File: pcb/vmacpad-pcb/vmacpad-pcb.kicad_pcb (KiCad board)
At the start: 2 copper layers, 134.7 x 126.1 mm, 79 parts, among them J1 TYPE-C-31-M12_13, J2 Conn_01x04_Pin, J3 Conn_01x04_Pin, K1 1u, K10 1u, K12 2.25u, K13 1u, K14 1u, K16 1u, K17 1u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

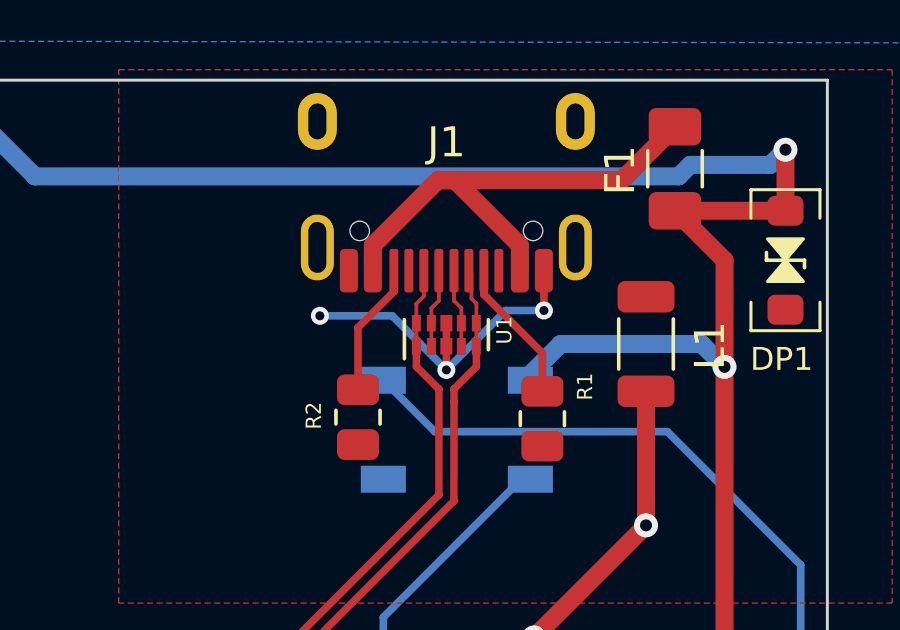
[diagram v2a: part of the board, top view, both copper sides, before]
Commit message: FIX USB connection
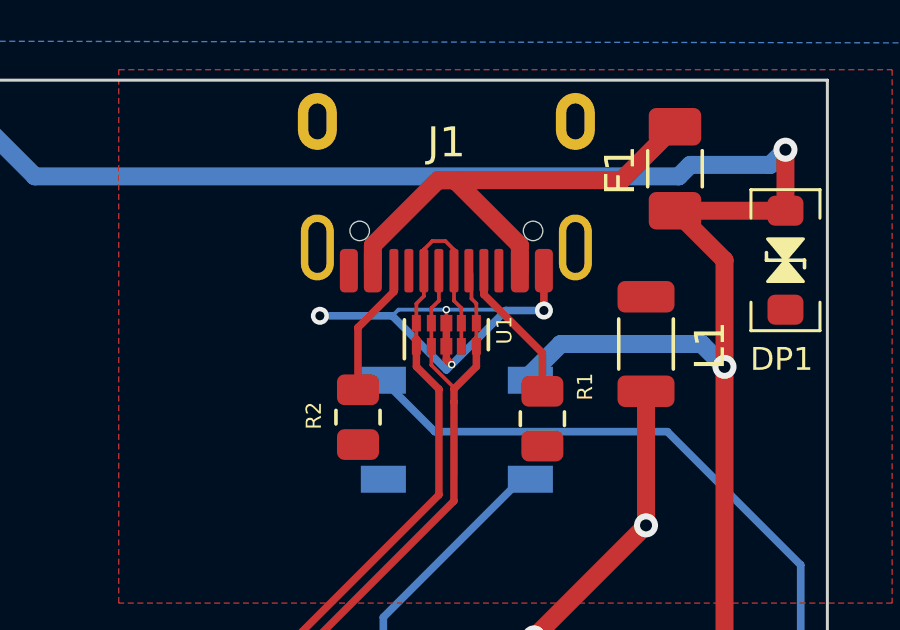
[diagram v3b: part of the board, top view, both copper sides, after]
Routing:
- net GNDPWR: track 11.9 -> 16.1 mm, vias 3 -> 4
- net USB+: track 158.8 -> 161.5 mm
- net USB-: track 159.5 -> 161.3 mm
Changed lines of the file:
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@@
   (via (at 130.7325 181.991) (size 0.6) (drill 0.3) (layers "F.Cu" "B.Cu") (net 3))
   (segment (start 114.3 196.342) (end 114.3 196.215) (width 0.254) (layer "B.Cu") (net 3))
+  (segment (start 211.582 106.7562) (end 211.582 107.188) (width 0.254) (layer "F.Cu") (net 4))
   (segment (start 214.8332 105.5624) (end 214.8332 104.2367) (width 0.254) (layer "F.Cu") (net 4))
   (segment (start 214.8332 104.2367) (end 214.832 104.2355) (width 0.254) (layer "F.Cu") (net 4))
+  (segment (start 211.582 105.536615) (end 211.58015 105.534765) (width 0.127) (layer "F.Cu") (net 4))
+  (segment (start 211.582 105.9862) (end 211.582 105.536615) (width 0.127) (layer "F.Cu") (net 4))
   (segment (start 211.582 106.7562) (end 211.582 105.9862) (width 0.254) (layer "F.Cu") (net 4))
-  (segment (start 211.582 106.7562) (end 211.582 107.5436) (width 0.254) (layer "F.Cu") (net 4))
+  (segment (start 211.582 107.188) (end 211.7598 107.3658) (width 0.254) (layer "F.Cu") (net 4))
   (via (at 214.8332 105.5624) (size 0.6) (drill 0.3) (layers "F.Cu" "B.Cu") (net 4))
   (via (at 207.3656 105.7402) (size 0.6) (drill 0.3) (layers "F.Cu" "B.Cu") (net 4))
-  (via (at 211.582 107.5436) (size 0.6) (drill 0.3) (layers "F.Cu" "B.Cu") (net 4))
+  (via (at 211.58015 105.534765) (size 0.25) (drill 0.15) (layers "F.Cu" "B.Cu") (net 4))
+  (via (at 211.7598 107.3658) (size 0.25) (drill 0.15) (layers "F.Cu" "B.Cu") (net 4))
   (segment (start 211.582 107.5436) (end 209.7786 105.7402) (width 0.254) (layer "B.Cu") (net 4))
-  (segment (start 211.582 107.5436) (end 213.5632 105.5624) (width 0.254) (layer "B.Cu") (net 4))
+  (segment (start 213.535565 105.534765) (end 213.5632 105.5624) (width 0.127) (layer "B.Cu") (net 4))
+  (segment (start 211.582 107.5436) (end 211.7598 107.3658) (width 0.254) (layer "B.Cu") (net 4))
   (segment (start 209.7786 105.7402) (end 207.3656 105.7402) (width 0.254) (layer "B.Cu") (net 4))
+  (segment (start 211.58015 105.534765) (end 209.984035 105.534765) (width 0.127) (layer "B.Cu") (net 4))
   (segment (start 213.5632 105.5624) (end 214.8332 105.5624) (width 0.254) (layer "B.Cu") (net 4))
+  (segment (start 211.7598 107.3658) (end 213.5632 105.5624) (width 0.254) (layer "B.Cu") (net 4))
+  (segment (start 211.58015 105.534765) (end 213.535565 105.534765) (width 0.127) (layer "B.Cu") (net 4))
+  (segment (start 209.984035 105.534765) (end 209.7786 105.7402) (width 0.127) (layer "B.Cu") (net 4))
   (segment (start 214.7824 108.2567) (end 214.7824 106.979414) (width 0.254) (layer "F.Cu") (net 5))
   (segment (start 212.832 105.029014) (end 212.832 104.2355) (width 0.254) (layer "F.Cu") (net 5))
@@
   (segment (start 210.582 105.3342) (end 210.582 105.7362) (width 0.127) (layer "F.Cu") (net 77))
   (segment (start 196.7016 126.337646) (end 211.333502 111.705744) (width 0.25) (layer "F.Cu") (net 77))
+  (segment (start 210.832 103.531789) (end 210.832 104.2355) (width 0.127) (layer "F.Cu") (net 77))
   (segment (start 120.2984 165.860046) (end 125.880446 160.278) (width 0.25) (layer "F.Cu") (net 77))
   (segment (start 196.7016 144.879646) (end 196.7016 126.337646) (width 0.25) (layer "F.Cu") (net 77))
+  (segment (start 211.116789 103.247) (end 210.832 103.531789) (width 0.127) (layer "F.Cu") (net 77))
   (segment (start 212.082 105.4842) (end 212.082 105.9862) (width 0.127) (layer "F.Cu") (net 77))
   (segment (start 181.303246 160.278) (end 196.7016 144.879646) (width 0.25) (layer "F.Cu") (net 77))
@@
   (segment (start 210.582 107.4326) (end 210.582 106.5062) (width 0.25) (layer "F.Cu") (net 77))
   (segment (start 210.582 105.7362) (end 210.582 106.5062) (width 0.127) (layer "F.Cu") (net 77))
+  (segment (start 211.836 104.2355) (end 211.836 103.535789) (width 0.127) (layer "F.Cu") (net 77))
   (segment (start 210.832 105.0842) (end 210.582 105.3342) (width 0.127) (layer "F.Cu") (net 77))
   (segment (start 115.2125 185.86875) (end 118.425296 185.86875) (width 0.25) (layer "F.Cu") (net 77))
+  (segment (start 211.547211 103.247) (end 211.116789 103.247) (width 0.127) (layer "F.Cu") (net 77))
   (segment (start 211.333502 108.184102) (end 210.582 107.4326) (width 0.25) (layer "F.Cu") (net 77))
   (segment (start 211.836 104.2355) (end 211.836 105.2382) (width 0.127) (layer "F.Cu") (net 77))
+  (segment (start 211.836 103.535789) (end 211.547211 103.247) (width 0.127) (layer "F.Cu") (net 77))
   (segment (start 211.836 105.2382) (end 212.082 105.4842) (width 0.127) (layer "F.Cu") (net 77))
   (segment (start 212.082 105.9862) (end 212.082 106.7562) (width 0.127) (layer "F.Cu") (net 77))
@@
   (segment (start 210.832 104.2355) (end 210.832 105.0842) (width 0.127) (layer "F.Cu") (net 77))
   (segment (start 212.4185 105.167764) (end 212.4185 104.322) (width 0.127) (layer "F.Cu") (net 78))
+  (segment (start 211.082 107.383178) (end 211.836 108.137178) (width 0.127) (layer "F.Cu") (net 78))
   (segment (start 118.632404 186.36875) (end 120.7984 184.202754) (width 0.25) (layer "F.Cu") (net 78))
   (segment (start 211.332 105.2342) (end 211.082 105.4842) (width 0.127) (layer "F.Cu") (net 78))
@@
   (segment (start 212.582 105.9862) (end 212.582 106.7562) (width 0.127) (layer "F.Cu") (net 78))
   (segment (start 211.836 108.6104) (end 211.836 108.1786) (width 0.25) (layer "F.Cu") (net 78))
+  (segment (start 211.082 106.7562) (end 211.082 107.383178) (width 0.127) (layer "F.Cu") (net 78))
+  (segment (start 211.836 108.137178) (end 211.836 108.1786) (width 0.127) (layer "F.Cu") (net 78))
   (segment (start 212.582 105.9862) (end 212.582 105.331264) (width 0.127) (layer "F.Cu") (net 78))
   (segment (start 211.833502 111.912852) (end 211.836 108.6104) (width 0.25) (layer "F.Cu") (net 78))

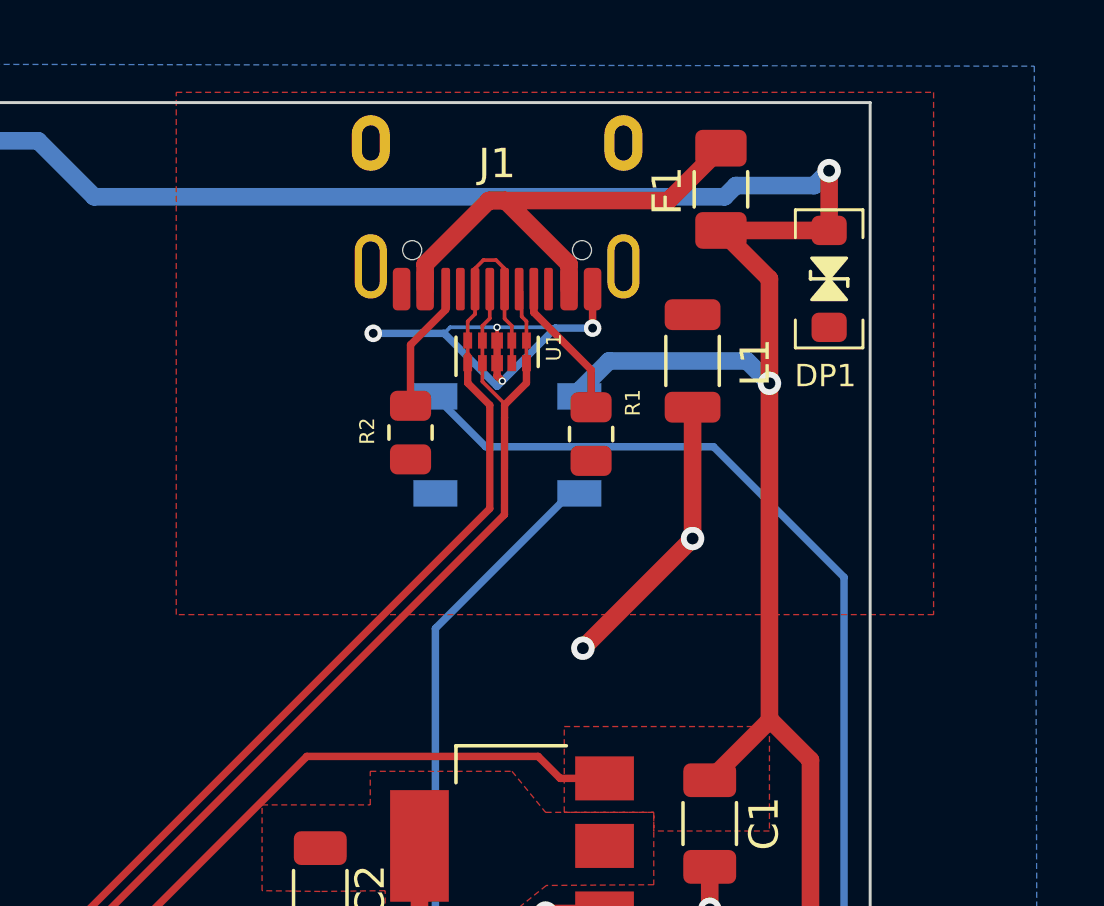
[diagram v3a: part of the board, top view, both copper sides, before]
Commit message: Improve USB component placement
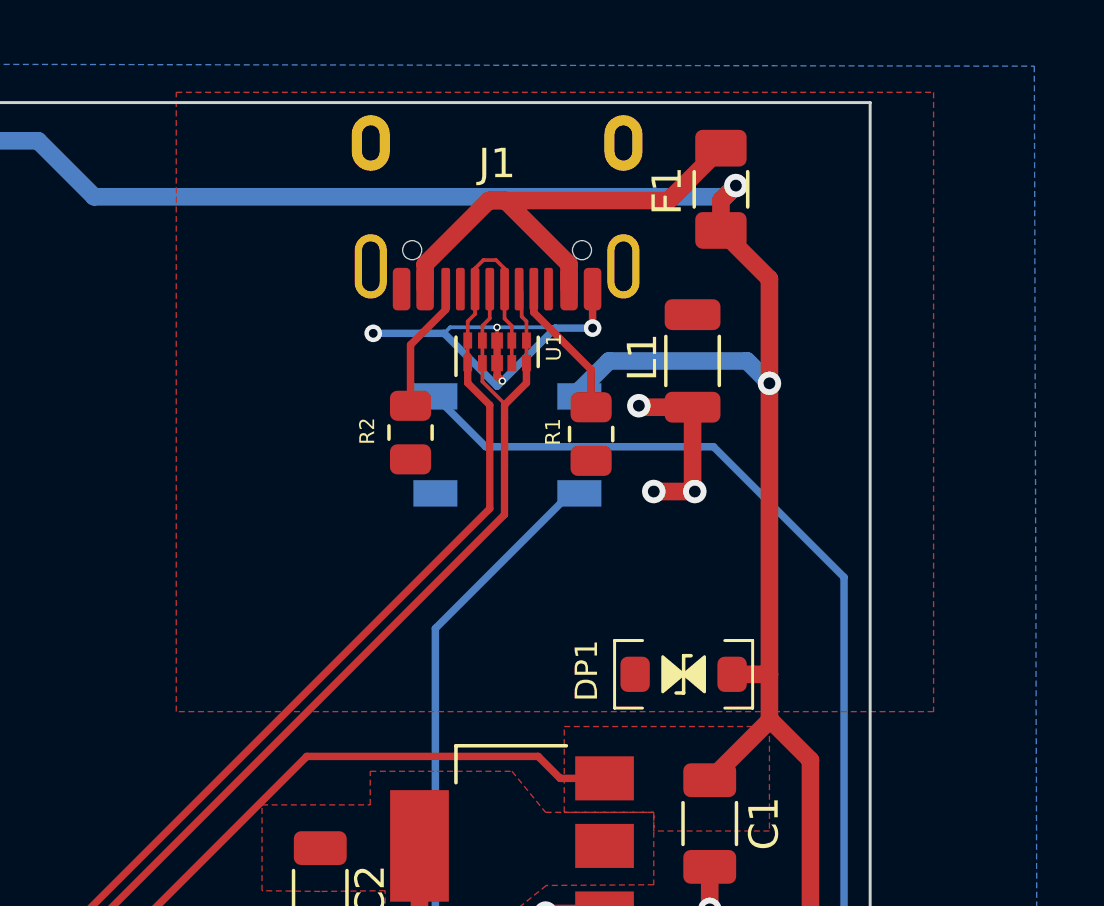
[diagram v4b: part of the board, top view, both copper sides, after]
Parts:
- moved DP1 14.3 mm to (217.9, 117.3), turned to 0 degrees
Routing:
- net VCC: track 381.4 -> 375.3 mm
- net GND: track 64.7 -> 60.8 mm, vias 26 -> 27
